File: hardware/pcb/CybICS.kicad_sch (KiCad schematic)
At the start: 75 parts, among them J1 Raspberry_Pi_2_3, J2 Conn_01x03_Pin, J3 Conn_01x05_Pin, SW1 SW_Push, SW2 SW_Push, SW3 SW_Push, U1 STM32G070RBTx

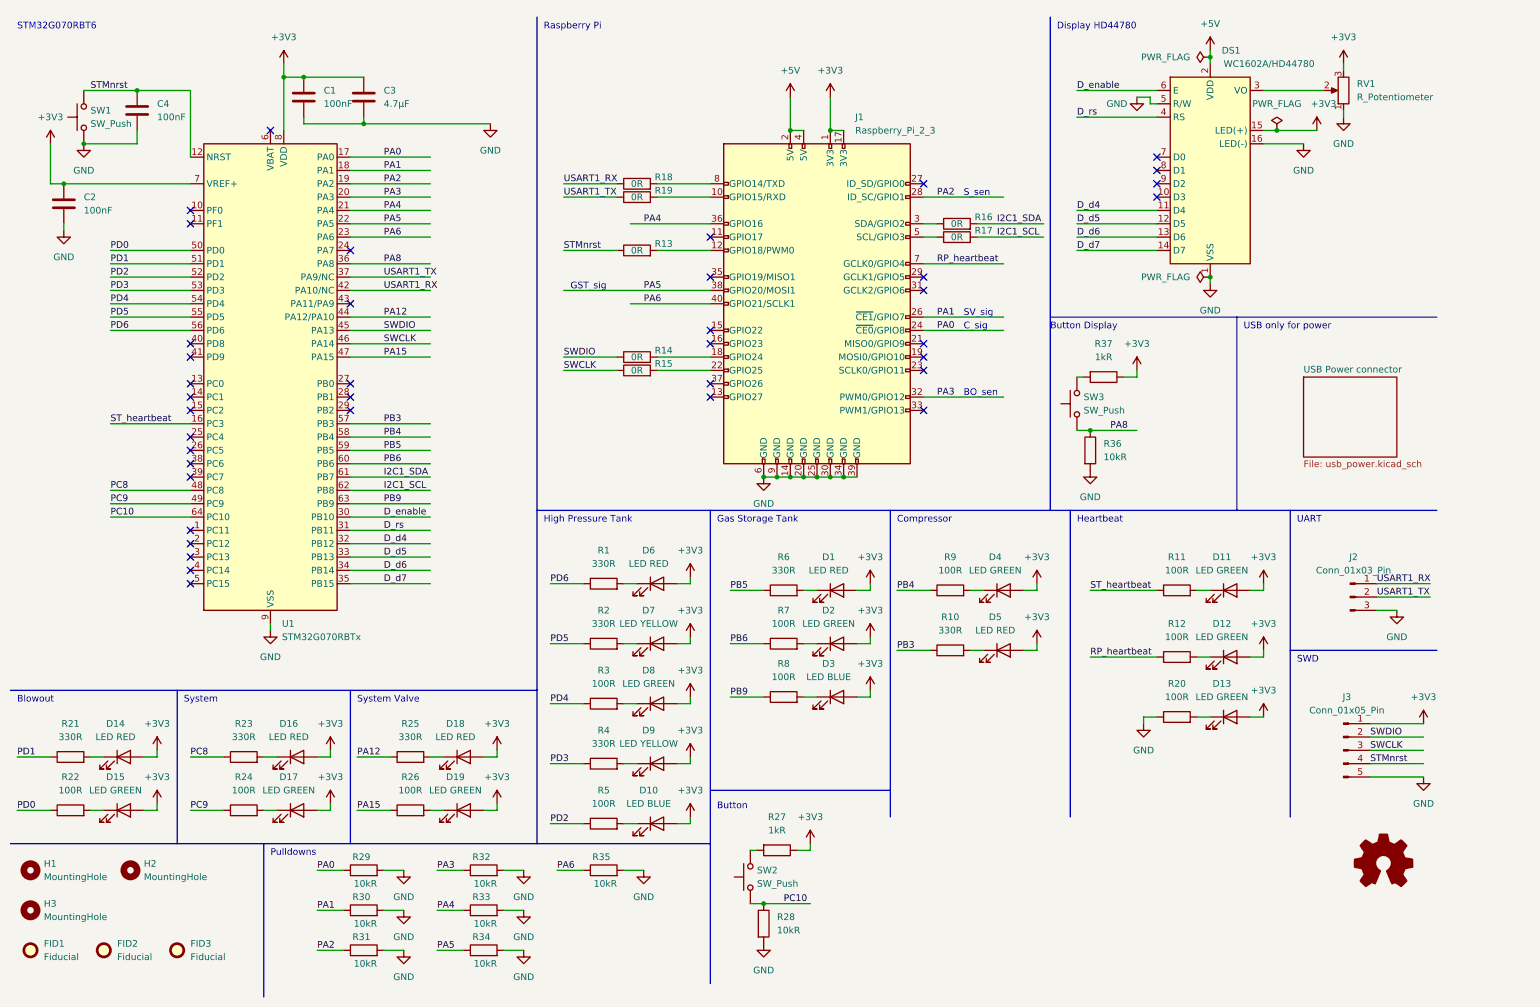
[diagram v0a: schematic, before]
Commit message: feat(hardware): add a 5-bit hardware version strap to the STM32 and the Pi
A new board revision needs to be identifiable from software, so both
controllers get a version code they can read back.

One 10k resistor per bit to GND, read against the controller's internal
pull-up: fitted = 0, omitted = 1. That keeps it to a single part per bit,
and future revisions are then a pure assembly change -- no schematic or
layout edit to bump the version. The value is C17414, which the board
already carries nine times, so the BOM gains no line and no feeder fee;
the ten straps group into the existing 10kR row (R28-R36,R40-R44,R46-R50).

Pins were picked for contiguity on the board rather than in the
schematic, because routing was the constraint:

  HWV_STM0..4  U1 pins 1-5    PC11, PC12, PC13, PC14, PC15
  HWV_RPI0..4  J1 11,13,15    GPIO17, GPIO27, GPIO22
               J1 16,19       GPIO23, GPIO10

PC14/PC15 are the LSE oscillator pins and PF0/PF1 the HSE pins; the board
fits no crystal, so the former are free to use and the latter were still
left alone. SPI0 clock and ID_SD/GPIO0 (reserved for the HAT EEPROM) were
kept clear; GPIO10 is MOSI0 and is the one compromise, taken because the
corridor south of J1 pins 23/29/31 is blocked by the LCD's fan-out.

All ten straps route north to their pin and drop south through a via into
the B.Cu GND plane, so the ground side needed no routing at all.

Nothing else was rewired, and that is checked rather than asserted: of
the 108 nets the design had before, 107 have byte-identical node sets
afterwards. The single exception is GND, which gained ten nodes and lost
none. The ten new nets carry exactly two nodes each.

Designators sit north of their parts at 3.6 mm, rotated vertical. The
library default put them 1.65 mm east, where they collided with the next
resistor in the 2 mm pitch; 2.5 mm north still placed every label over
its own pad, where the silkscreen would have been clipped in production.
Silkscreen warnings across the board dro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
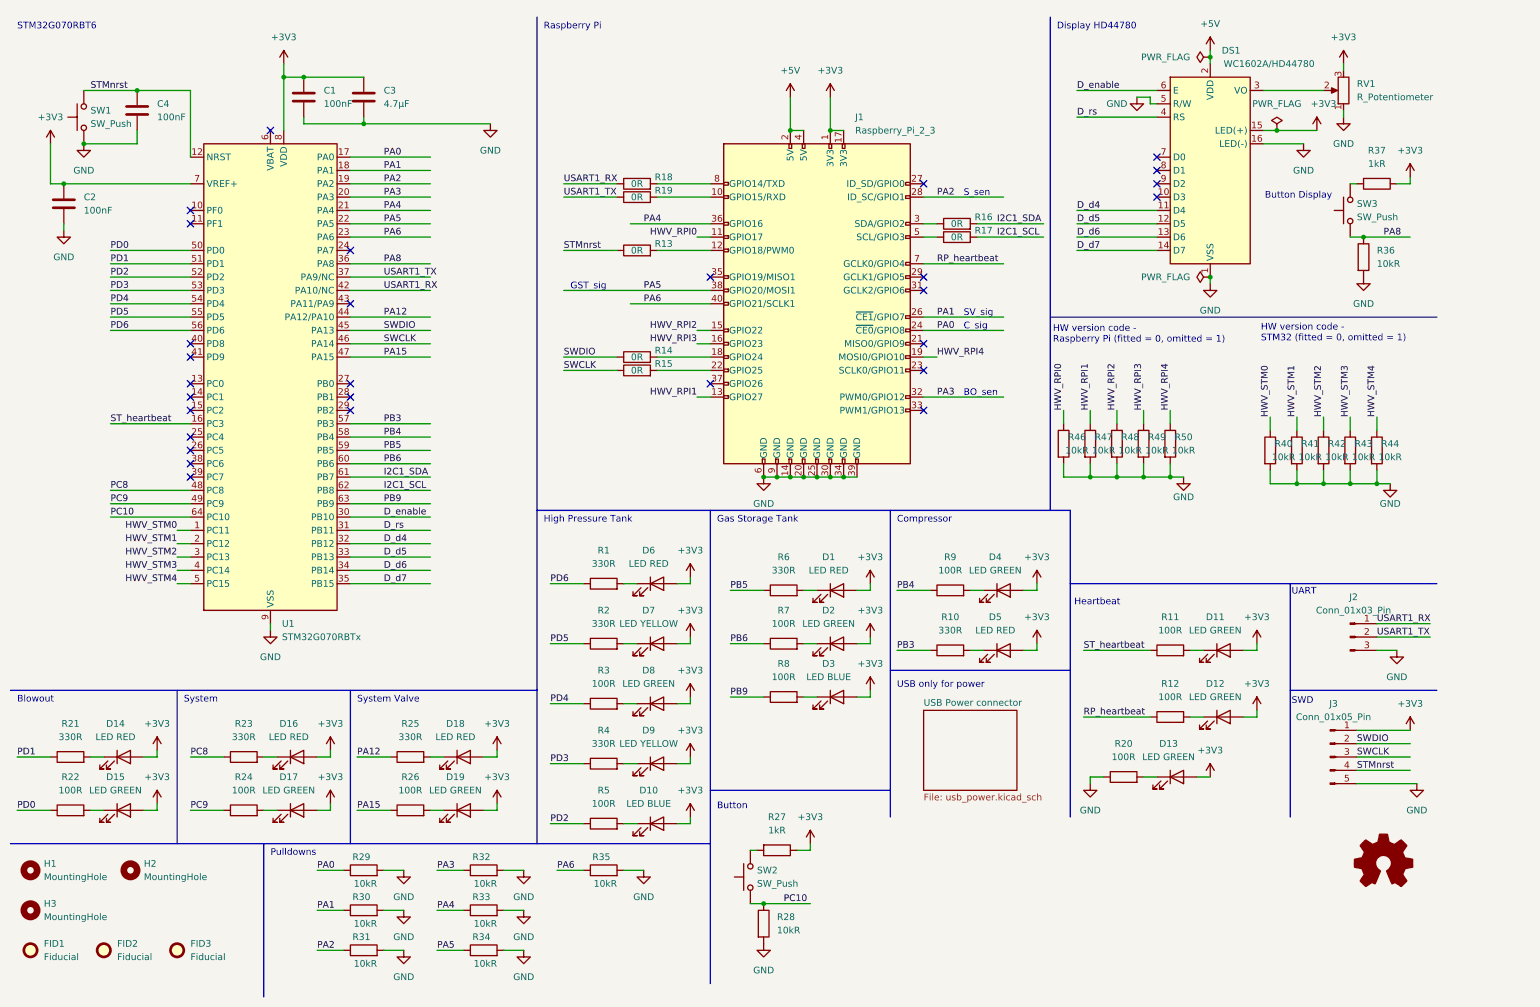
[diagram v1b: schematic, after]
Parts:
- added R40, R41, R42, R43, R44, R46, R47, R48, R49, R50: 10kR, Resistor_SMD:R_0805_2012Metric_Pad1.20x1.40mm_HandSolder, symbol Device:R
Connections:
- net GND: now also R40.2, R41.2, R42.2, R43.2, R44.2, R46.2, R47.2, R48.2, R49.2, R50.2
- net HWV_RPI0: now reaches J1.11 (GPIO17)
- net HWV_RPI0: now also R46.1
- net HWV_RPI1: now reaches J1.13 (GPIO27)
- net HWV_RPI1: now also R47.1
- net HWV_RPI2: now reaches J1.15 (GPIO22)
- net HWV_RPI2: now also R48.1
- net HWV_RPI3: now reaches J1.16 (GPIO23)
- net HWV_RPI3: now also R49.1
- net HWV_RPI4: now reaches J1.19 (MOSI0/GPIO10)
- net HWV_RPI4: now also R50.1
- net HWV_STM0: now reaches U1.1 (PC11)
- net HWV_STM0: now also R40.1
- net HWV_STM1: now reaches U1.2 (PC12)
- net HWV_STM1: now also R41.1
- net HWV_STM2: now reaches U1.3 (PC13)
- net HWV_STM2: now also R42.1
- net HWV_STM3: now reaches U1.4 (PC14)
- net HWV_STM3: now also R43.1
- net HWV_STM4: now reaches U1.5 (PC15)
- net HWV_STM4: now also R44.1
- no-connect marks 39 -> 29
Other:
- note added: "HW version code - Raspberry Pi (fitted = 0, omitted = 1)"
- note added: "HW version code - STM32 (fitted = 0, omitted = 1)"
- moved on the sheet: D11, D12, D13, J2, J3, R11, R12, R20, R36, R37, SW3

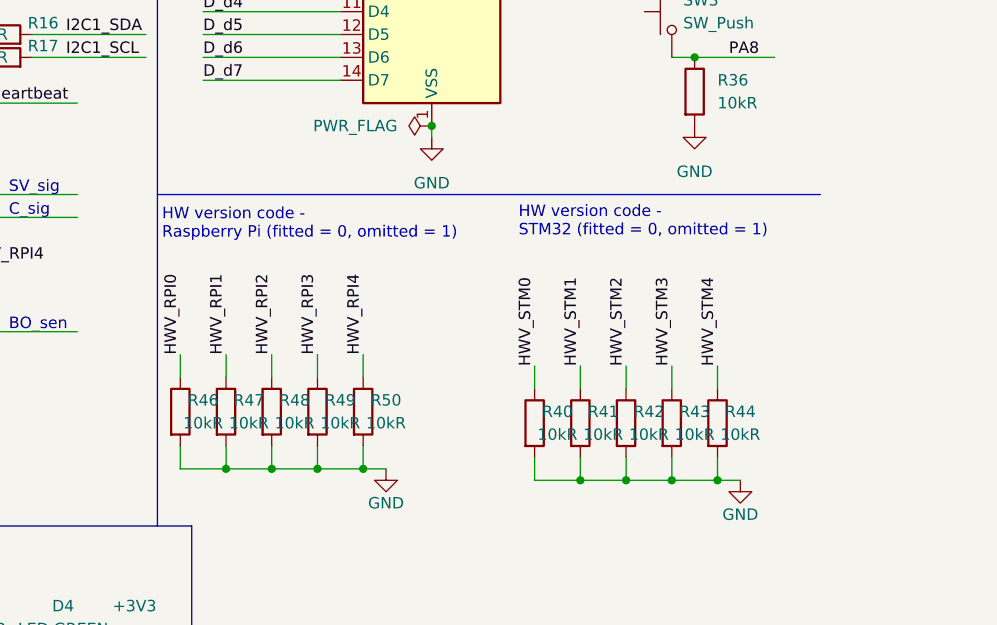
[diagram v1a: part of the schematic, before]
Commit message: feat(hardware)!: encode this revision as hardware version 1.1
The straps from the previous commit were all fitted, so both controllers
reported code 0. This assigns the revision properly: bit 0 is omitted on
each side (R40 for the STM32, R46 for the Pi), giving `00001` = 1 = v1.1.
One resistor per side, because the two controllers read independent 5-bit
sets and must agree on the version.

The copper lettering moves with it: "CybICS v1.0" -> "CybICS v1.1" on
F.Cu and its F.Mask opening, so the board states its own revision.

Worth recording why 31 is reserved rather than used: a v1.0 board has no
strap footprints at all, so those pins float and the internal pull-ups
make it read `11111`. Every pre-v1.1 board therefore identifies itself
without any change to it, which is the useful half. The other half is
that a v1.1 board assembled with no straps reads the same, so 31 means
"pre-v1.1, or straps missing" and cannot be given to a real revision.

R40 and R46 carry `(dnp yes)` in the schematic and `dnp` in the footprint
attributes. Verified both ways with kicad-cli 10.0.6: `sch export bom
--exclude-dnp` yields R28-R36,R41-R44,R47-R50 with R40/R46 gone, and
without the flag they appear marked DNP; `pcb export pos --exclude-dnp`
gives 74 rows against 76 without it, with R40 and R46 absent. Whether
JLCPCB actually receives them depends on the Fabrication Toolkit
honouring DNP, so the ordering guide now has an explicit check for it --
if they get placed, the board reports the wrong revision.

Documented in hardware/README.md with the bit-to-pin table and the code
table, and CLAUDE.md gains the F8 trap found while verifying this: Update
PCB from Schematic resets footprint attributes from the library and
silently drops exclude_from_pos_files from FID1-FID3 and H1-H3, which
puts the #238 fiducials straight back into the position file.

Verified: ERC, DRC and schematic parity all 0 violations and 0
unconnected items after the copper lettering change; all four
kibotVerify.yml ge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
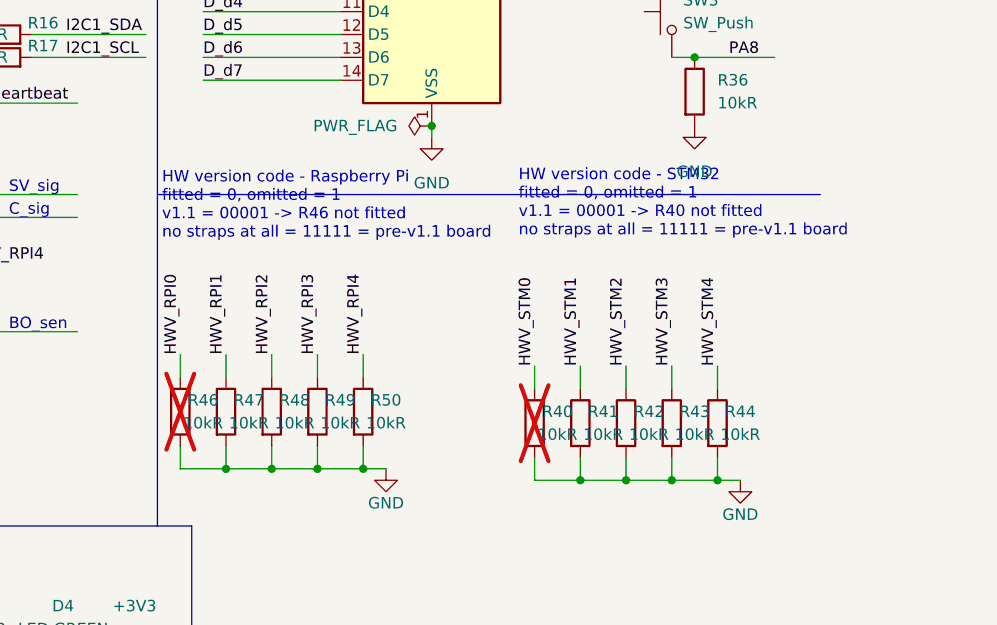
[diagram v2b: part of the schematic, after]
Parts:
- R40, R46: now not fitted
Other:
- note added: "HW version code - Raspberry Pi fitted = 0, omitted = 1 v1.1 = 00001 -> R46 not fitted no straps at all = 11111 = pre-v1.1 board"
- note added: "HW version code - STM32 fitted = 0, omitted = 1 v1.1 = 00001 -> R40 not fitted no straps at all = 11111 = pre-v1.1 board"
- note removed: "HW version code - Raspberry Pi (fitted = 0, omitted = 1)"
- note removed: "HW version code - STM32 (fitted = 0, omitted = 1)"
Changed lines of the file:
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@@
 		)
 	)
-	(text "HW version code - \nSTM32 (fitted = 0, omitted = 1)"
+	(text "HW version code - STM32\nfitted = 0, omitted = 1\nv1.1 = 00001 -> R40 not fitted\nno straps at all = 11111 = pre-v1.1 board"
 		(exclude_from_sim no)
 		(at 250.952 74.676 0)
@@
 		)
 	)
-	(text "HW version code - \nRaspberry Pi (fitted = 0, omitted = 1)"
+	(text "HW version code - Raspberry Pi\nfitted = 0, omitted = 1\nv1.1 = 00001 -> R46 not fitted\nno straps at all = 11111 = pre-v1.1 board"
 		(exclude_from_sim no)
 		(at 211.328 74.93 0)
@@
 		(on_board yes)
 		(in_pos_files yes)
-		(dnp no)
+		(dnp yes)
 		(fields_autoplaced yes)
 		(property "Reference" "R46"
@@
 		(on_board yes)
 		(in_pos_files yes)
-		(dnp no)
+		(dnp yes)
 		(fields_autoplaced yes)
 		(property "Reference" "R40"

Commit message: feat(hardware)!: replace the display button with the 4-way navigation switch
SW3 becomes the SHOU HAN 7*7*5-6P-L WX (C2858287): four directions plus a
centre press on a shared common. Schematic only -- the board still has
the old SW_Push footprint until Update PCB from Schematic is run.

The drive scheme gets simpler rather than more complex. The old button
sat between R37 (1k to +3V3) and R36 (10k to GND) and read active high;
repeating that for five contacts would have meant ten resistors. Instead
the common goes to GND and the five contacts are read with the STM32's
internal pull-ups, the same approach as the version straps -- so R36 and
R37 are gone and no resistor replaces them.

Pin choice keeps the existing net where it helps: F1 stays on PA8, so
"the display button" is still PA8 for firmware, while F2..F5 take PC4,
PC5, PB0 and PB1 -- pins 25-28, contiguous on the south edge of the MCU.
16 usable free pins remain afterwards.

The two unnamed anchor tabs (pins 7 and 8) are deliberately left
unconnected. Tying them to GND is the usual treatment for mechanical
tabs, but the vendor data does not say they are purely mechanical, and
an unconnected pad cannot short a contact while a grounded one can.

The library symbol was renamed from the EasyEDA original `7*7*5-6P-LWX`
to `SW_Nav_4Way_7x7`: asterisks are wildcards in KiCad library lookups
and the original name is unreadable in a schematic.

Verified with kicad-cli 10.0.6: ERC reports 0 violations. The netlist
diff shows exactly what was intended -- /PA8 is now SW3.5 plus U1.36,
the four new nets carry exactly two nodes each (SW3 contact and MCU pin),
GND gained SW3.2 and lost R36.2, +3V3 lost R37.1, and pins 7/8 show as
unconnected. The BOM lists SW3 as C2858287 while SW1/SW2 keep C428628,
which is the one extra extended part this costs.

Note on parity checking: `kicad-cli pcb drc --schematic-parity` silently
reports zero when run from outside the project directory, because it
cannot resolve the schematic. Run 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
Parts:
- removed R36: 10kR, Resistor_SMD:R_0805_2012Metric_Pad1.20x1.40mm_HandSolder, symbol Device:R
- removed R37: 1kR, Resistor_SMD:R_0805_2012Metric_Pad1.20x1.40mm_HandSolder, symbol Device:R
- removed SW3: SW_Push, Button_Switch_THT:SW_PUSH_6mm_H5mm, symbol Switch:SW_Push
- added SW3: 7*7*5-6P-L WX, cybics:SW-SMD_8P-L7.0-W7.0-P1.40-LS7.4-TL, symbol cybics:SW_Nav_4Way_7x7
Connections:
- net GND: now also SW3.2 (Public)
- net PA8: now also SW3.5 (F1)
- net NAV_F2: now reaches U1.25 (PC4)
- net NAV_F2: now also SW3.1 (F2)
- net NAV_F4: now reaches U1.26 (PC5)
- net NAV_F4: now also SW3.3 (F4)
- net NAV_F3: now reaches U1.27 (PB0)
- net NAV_F3: now also SW3.6 (F3)
- net NAV_F5: now reaches U1.28 (PB1)
- net NAV_F5: now also SW3.4 (F5)
- no-connect marks 29 -> 27
